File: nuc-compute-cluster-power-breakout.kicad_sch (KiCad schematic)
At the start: 44 parts

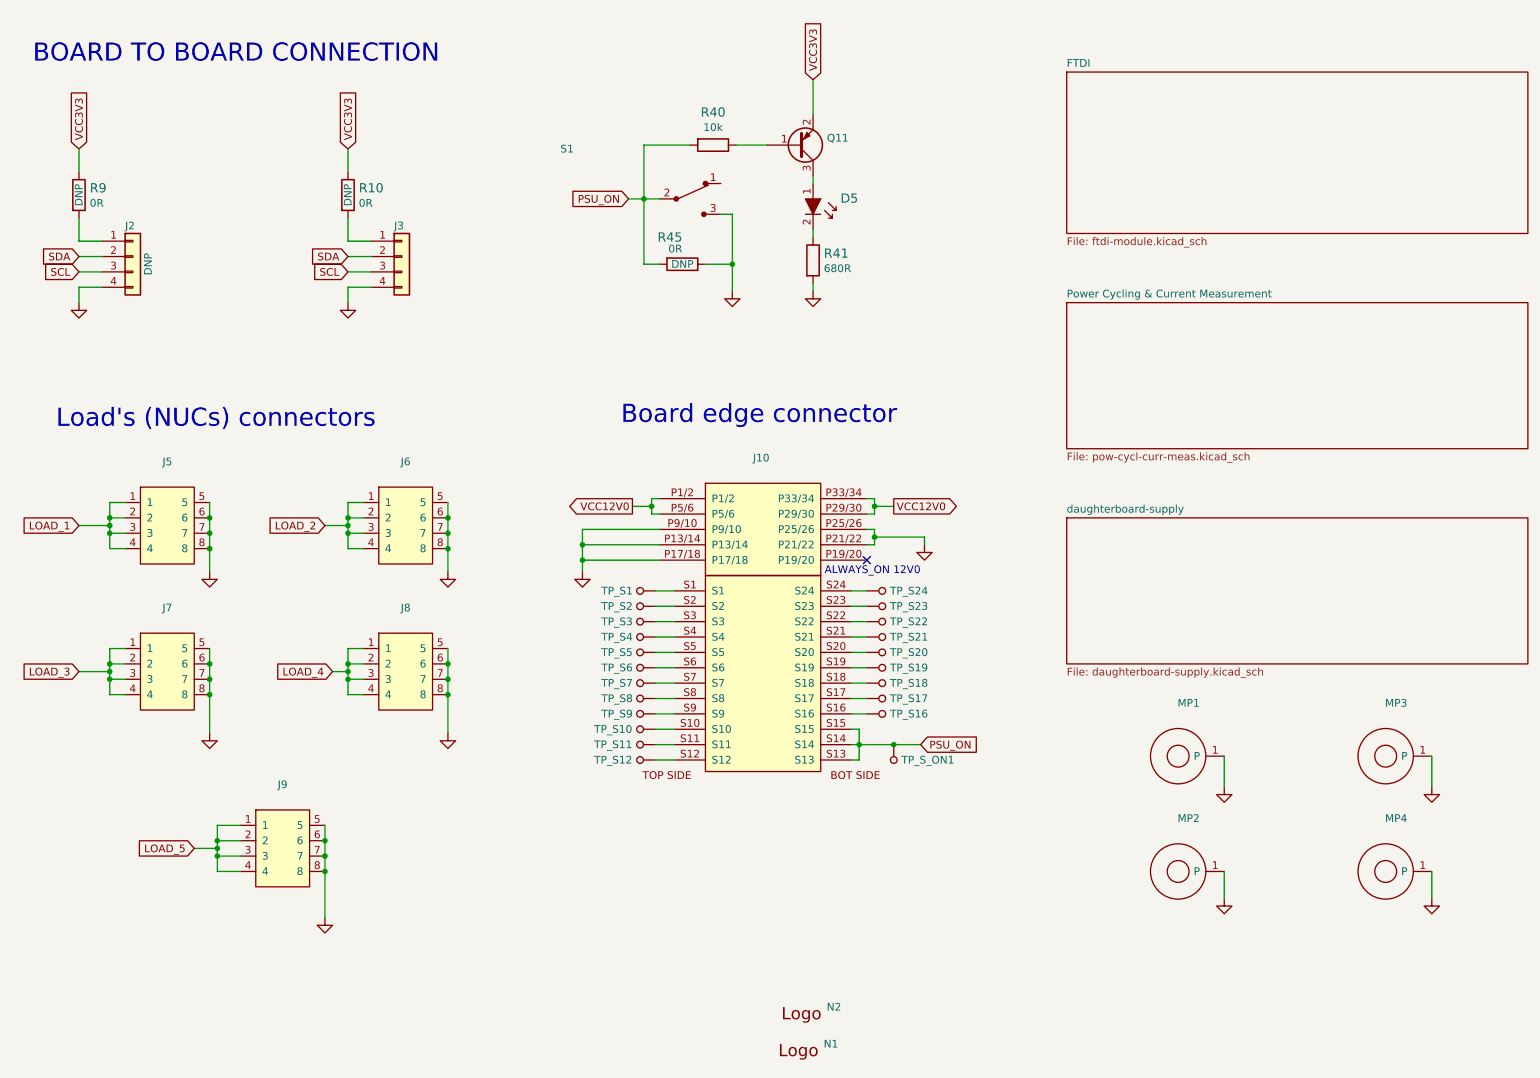
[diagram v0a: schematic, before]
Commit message: Fixed FTDI sheet
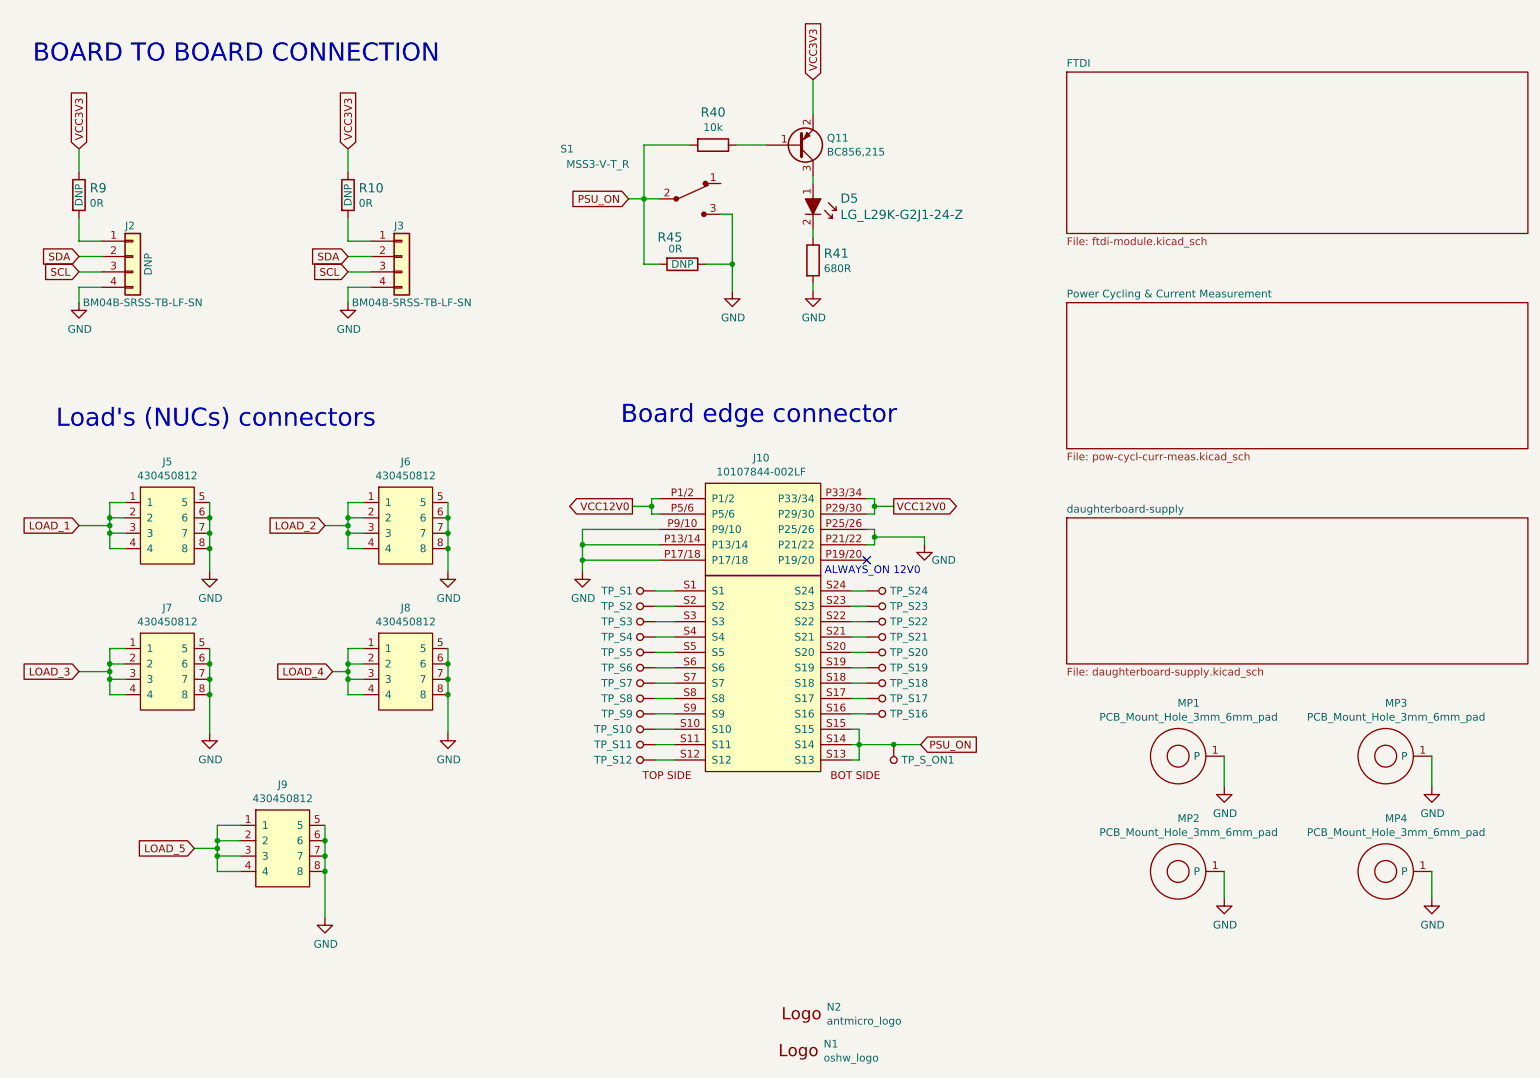
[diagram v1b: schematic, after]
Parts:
- D5: value (none) -> LG_L29K-G2J1-24-Z; footprint (none) -> nuc-compute-cluster-power-breakout-footprints:LED_0603
- J10: value (none) -> 10107844-002LF; footprint (none) -> nuc-compute-cluster-power-breakout-footprints:10107844-002LF
- J2, J3: value (none) -> BM04B-SRSS-TB-LF-SN; footprint (none) -> nuc-compute-cluster-power-breakout-footprints:BM04B-SRSS-TB-LF-SN
- J5, J6, J7, J8, J9: value (none) -> 430450812; footprint (none) -> nuc-compute-cluster-power-breakout-footprints:Molex-43045-0812
- MP1, MP2, MP3, MP4: value (none) -> PCB_Mount_Hole_3mm_6mm_pad; footprint (none) -> nuc-compute-cluster-power-breakout-footprints:mounting-hole-3.2mm
- N1: value (none) -> oshw_logo; footprint (none) -> nuc-compute-cluster-power-breakout-footprints:OSHW-Logo_7.5x8mm_Mask
- N2: value (none) -> antmicro_logo; footprint (none) -> nuc-compute-cluster-power-breakout-footprints:antmicro-logo_scaled_20mm_mask
- Q11: value (none) -> BC856,215; footprint (none) -> nuc-compute-cluster-power-breakout-footprints:SOT-23-3
- R10, R45, R9: value (none) -> R_0R_0402; footprint (none) -> nuc-compute-cluster-power-breakout-footprints:0402-res
- R40: value (none) -> R_10k_0402; footprint (none) -> nuc-compute-cluster-power-breakout-footprints:0402-res
- R41: value (none) -> R_680R_0402; footprint (none) -> nuc-compute-cluster-power-breakout-footprints:0402-res
- S1: value (none) -> MSS3-V-T_R; footprint (none) -> nuc-compute-cluster-power-breakout-footprints:Switch_Slide_MSS3
- TP_S1, TP_S10, TP_S11, TP_S12, TP_S16, TP_S17, TP_S18, TP_S19, TP_S2, TP_S20, TP_S21, TP_S22, TP_S23, TP_S24, TP_S3, TP_S4, TP_S5, TP_S6, TP_S7, TP_S8, TP_S9, TP_S_ON1: value (none) -> TP_SMD1MM; footprint (none) -> nuc-compute-cluster-power-breakout-footprints:Testpoint_smd_1mm

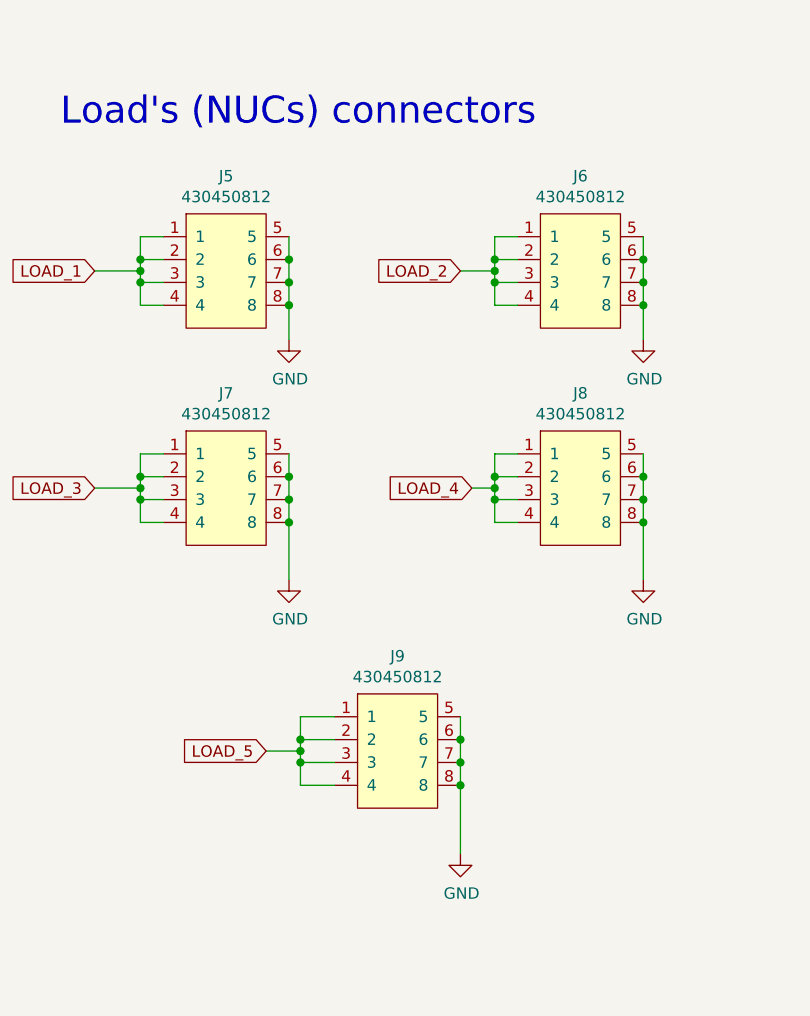
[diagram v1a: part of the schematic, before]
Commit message: Changed power connectors
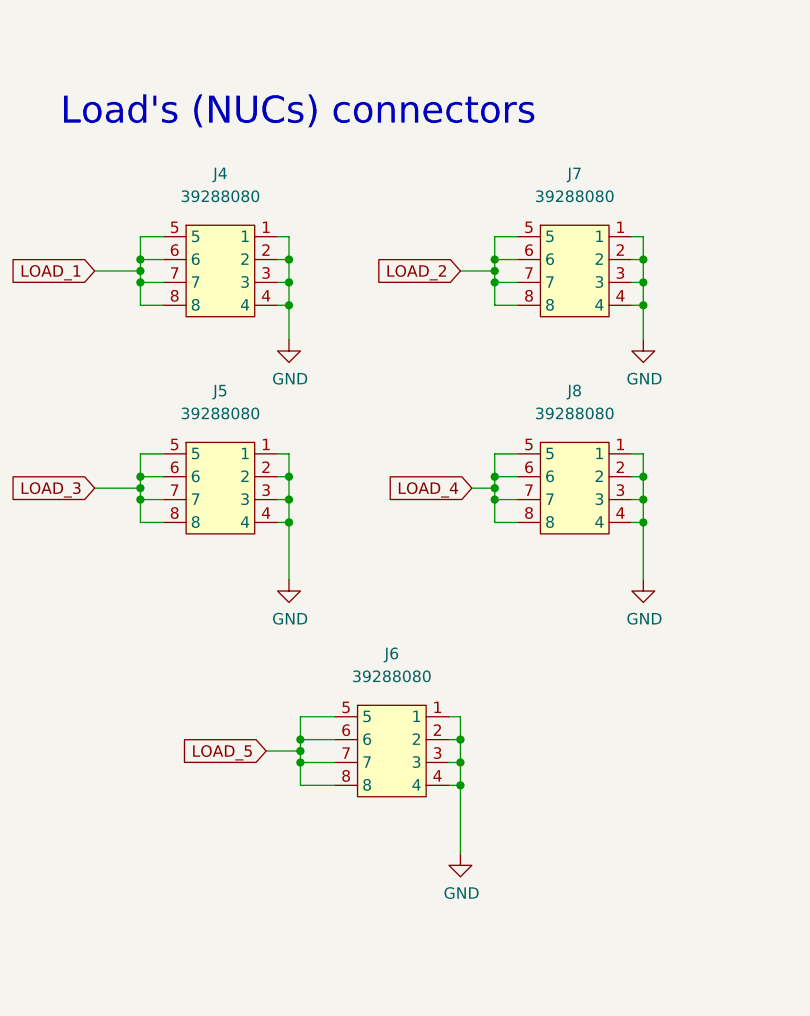
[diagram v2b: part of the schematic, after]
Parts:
- removed J5, J6, J7, J8, J9: 430450812, nuc-compute-cluster-power-breakout-footprints:Molex-43045-0812, symbol nuc-compute-cluster-power-breakout:430450812
- added J4, J5, J6, J7, J8: 39288080, antmicro-footprints:MOLEX_39288080, symbol antmicroRectangularConnectorsHeadersMalePins:39288080
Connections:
- net GND: now also J4.1, J4.2, J4.3, J4.4, J5.1, J5.2, J5.3, J5.4, J6.1, J6.2, J6.3, J6.4, J7.1, J7.2, J7.3, J7.4, J8.1, J8.2, J8.3, J8.4
- net LOAD_1: now also J4.5, J4.6, J4.7, J4.8
- net LOAD_2: now also J7.5, J7.6, J7.7, J7.8
- net LOAD_3: now also J5.5, J5.6, J5.7, J5.8
- net LOAD_4: now also J8.5, J8.6, J8.7, J8.8
- net LOAD_5: now also J6.5, J6.6, J6.7, J6.8

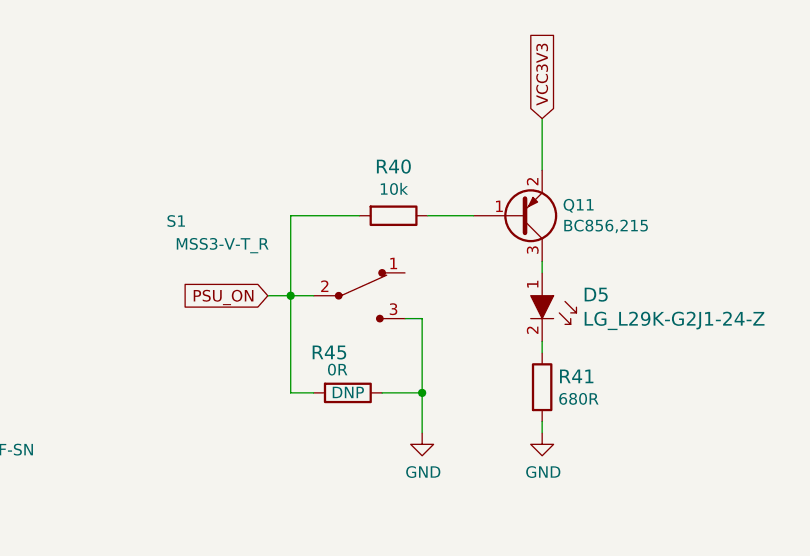
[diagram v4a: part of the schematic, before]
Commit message: Added support for default off and changed converter cap voltage rating
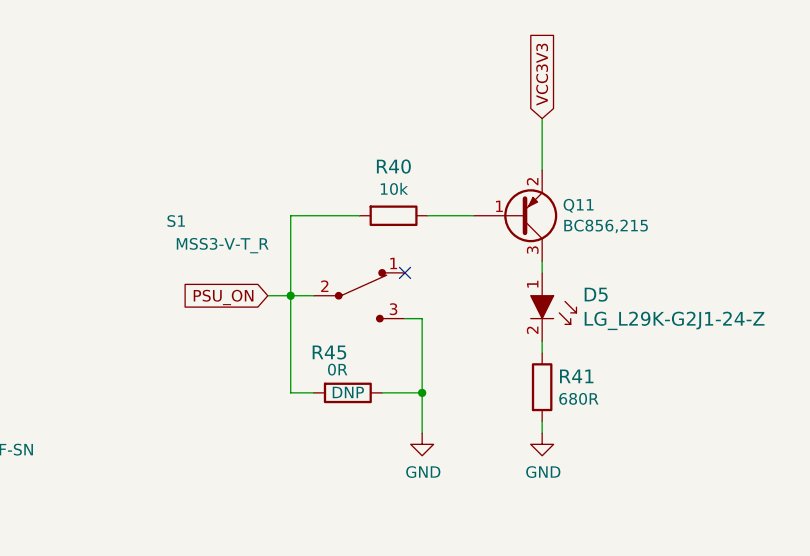
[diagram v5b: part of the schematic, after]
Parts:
- J4, J5, J6, J7, J8: footprint antmicro-footprints:MOLEX_39288080 -> nuc-compute-cluster-power-breakout-footprints:MOLEX_39288080; symbol antmicroRectangularConnectorsHeadersMalePins:39288080 -> nuc-compute-cluster-power-breakout:39288080
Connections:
- no-connect marks 1 -> 2
